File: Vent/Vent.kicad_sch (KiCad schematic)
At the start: 2 parts, among them J1 Conn_01x03, U1 ESP32-C3-WROOM-02-N4

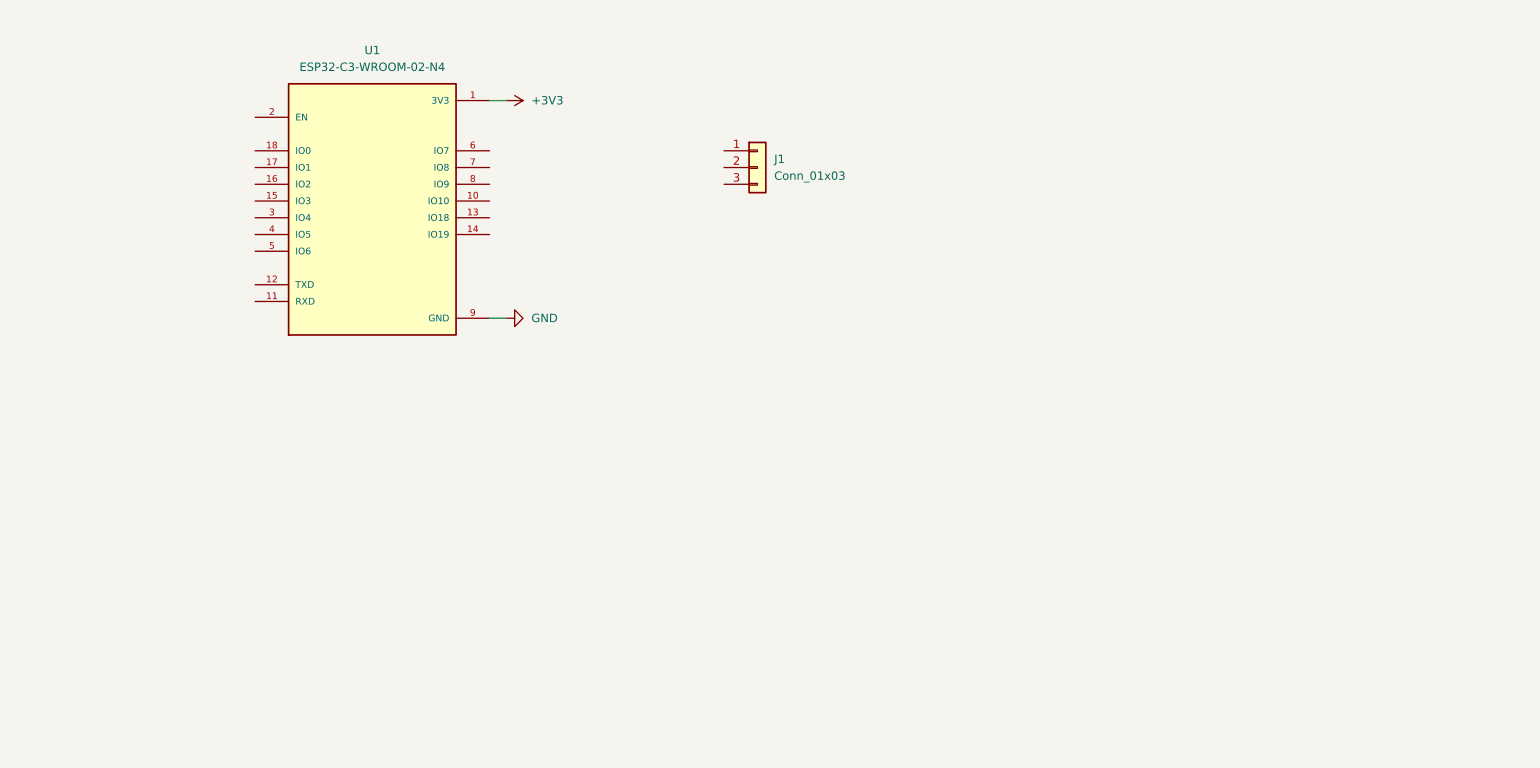
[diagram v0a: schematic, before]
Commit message: electronics: Sync latest designs from working directory
- Rename Puck board files (was Vent.kicad_* → Puck.kicad_*)
- Add full Comps libraries (footprints, models, symbols) for all four boards
- Add manufacturing-current/ Gerber outputs and renders for all boards
- Add new components: ESP32-C6-MINI-1 (Puck), ESP32-H2-MINI-1 (Vent), NCU15XH103F60RC (BMS)
- Add PCM JLCPCB passive symbol libraries across all boards
- Add per-project .gitignore files and Autoprogramming/AUTOPROGRAMMING_REVIEW.md
- Add root-level BOM files, sourcing audit, and manufacturing readiness ledger
- Update KiCad design files and Gerbers for BMS, Autoprogramming, and Vent

Co-Authored-By: Claude Sonnet 4.6 <noreply@anthropic.com>

Original-author: Zachariah K. Sharma <zachariah.sharma@gmail.com>
Source-commit: 261c676a3a26a8c60302274465dd756769088335
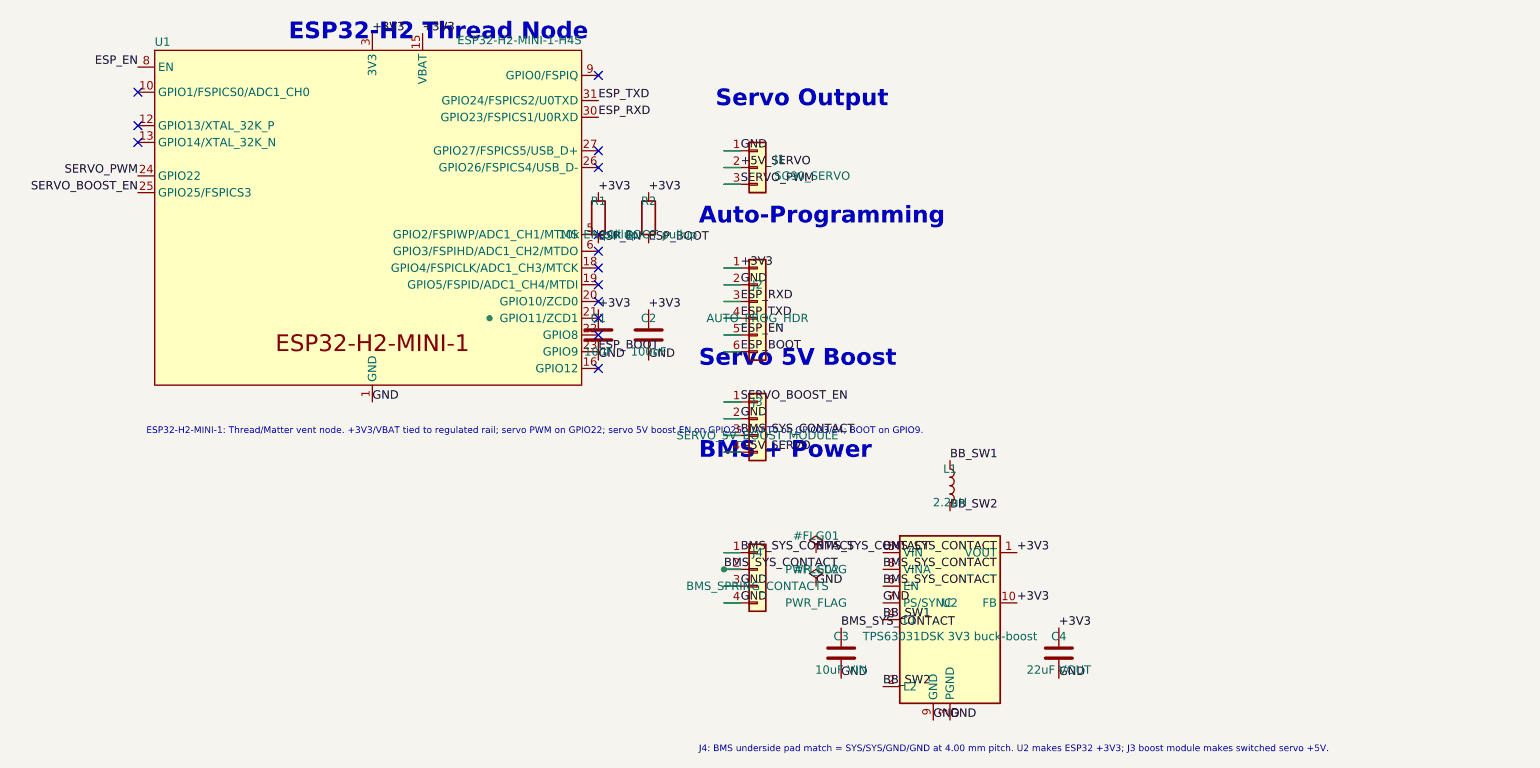
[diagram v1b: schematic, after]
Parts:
- removed U1: ESP32-C3-WROOM-02-N4, Footprints:MODULE_ESP32-C3-WROOM-02-H4, symbol ESP32-C3-WROOM-02-N4:ESP32-C3-WROOM-02-N4
- added C1: 10uF, Capacitor_SMD:C_0805_2012Metric, symbol Device:C
- added C2: 100nF, Capacitor_SMD:C_0603_1608Metric, symbol Device:C
- added C3: 10uF VIN, Capacitor_SMD:C_0805_2012Metric, symbol Device:C
- added C4: 22uF VOUT, Capacitor_SMD:C_0805_2012Metric, symbol Device:C
- added J2: AUTO_PROG_HDR, Connector_JST:JST_EH_B6B-EH-A_1x06_P2.50mm_Vertical, symbol Connector_Generic:Conn_01x06
- added J3: SERVO_5V_BOOST_MODULE, Footprints:PinHeader_1x04_P2.54mm_Vertical, symbol Connector_Generic:Conn_01x04
- added J4: BMS_SPRING_CONTACTS, VentPads:BMS_SpringLeafContacts_1x04_P4mm, symbol Connector_Generic:Conn_01x04
- added L1: 2.2uH, Inductor_SMD:L_1008_2520Metric, symbol Device:L
- added R1: 10k EN pullup, Resistor_SMD:R_0603_1608Metric, symbol Device:R
- added R2: 10k BOOT pullup, Resistor_SMD:R_0603_1608Metric, symbol Device:R
- added U1: ESP32-H2-MINI-1-H4S, Footprints:ESP32-H2-MINI-1, symbol ESP32-H2-MINI-1:ESP32-H2-MINI-1
- added U2: TPS63031DSK 3V3 buck-boost, Package_SON:WSON-10-1EP_2.5x2.5mm_P0.5mm_EP1.2x2mm, symbol Regulator_Switching:TPS63031DSK
- J1: value Conn_01x03 -> SG90_SERVO; footprint Connector_PinHeader_1.00mm:PinHeader_1x03_P1.00mm_Vertical -> Footprints:PinHeader_1x03_P2.54mm_Vertical; Pinout (none) -> 1=GND, 2=+5V_SERVO, 3=SERVO_PWM
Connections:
- net +3V3: now also C1.1, C2.1, C4.1, J2.1 (Pin_1), R1.1, R2.1, U1.15 (VBAT), U1.3 (3V3), U2.1 (VOUT), U2.10 (FB)
- net GND: now also J1.1 (Pin_1), C1.2, C2.2, C3.2, C4.2, J2.2 (Pin_2), J3.2 (Pin_2), J4.3 (Pin_3), J4.4 (Pin_4), U1.1 (GND), U1.11 (GND), U1.14 (GND), U1.2 (GND), U1.36 (GND), U1.37 (GND), U1.38 (GND), U1.39 (GND), U1.40 (GND), U1.41 (GND), U1.42 (GND), U1.43 (GND), U1.44 (GND), U1.45 (GND), U1.46 (GND), U1.47 (GND), U1.48 (GND), U1.49 (GND), U1.50 (GND), U1.51 (GND), U1.52 (GND), U1.53 (GND), U2.11 (PGND), U2.3 (PGND), U2.7 (PS/SYNC), U2.9 (GND)
- net +5V_SERVO: now reaches J1.2 (Pin_2)
- net +5V_SERVO: now also J3.4 (Pin_4)
- net SERVO_PWM: now reaches J1.3 (Pin_3)
- net SERVO_PWM: now also U1.24 (GPIO22)
- new net BB_SW1: L1.1, U2.4 (L1)
- new net BB_SW2: L1.2, U2.2 (L2)
- new net BMS_SYS_CONTACT: C3.1, J3.3 (Pin_3), J4.1 (Pin_1), J4.2 (Pin_2), U2.5 (VIN), U2.6 (EN), U2.8 (VINA)
- new net ESP_BOOT: J2.6 (Pin_6), R2.2, U1.23 (GPIO9)
- new net ESP_EN: J2.5 (Pin_5), R1.2, U1.8 (EN)
- new net ESP_RXD: J2.3 (Pin_3), U1.30 (GPIO23/FSPICS1/U0RXD)
- new net ESP_TXD: J2.4 (Pin_4), U1.31 (GPIO24/FSPICS2/U0TXD)
- new net SERVO_BOOST_EN: J3.1 (Pin_1), U1.25 (GPIO25/FSPICS3)
- no-connect marks 0 -> 14
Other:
- note added: "Auto-Programming"
- note added: "BMS + Power"
- note added: "ESP32-H2 Thread Node"
- note added: "ESP32-H2-MINI-1: Thread/Matter vent node. +3V3/VBAT tied to regulated rail; servo PWM on GPIO22; servo 5V boost EN on GPIO25; UART0 on GPIO23/24; BOOT on GPIO9."
- note added: "J4: BMS underside pad match = SYS/SYS/GND/GND at 4.00 mm pitch. U2 makes ESP32 +3V3; J3 boost module makes switched servo +5V."
- note added: "Servo 5V Boost"
- note added: "Servo Output"
